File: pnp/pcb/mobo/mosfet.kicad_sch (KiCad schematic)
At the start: 4 parts, among them J25 Mosfet, Q4 AO3400A

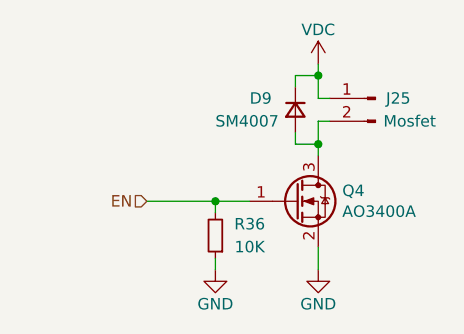
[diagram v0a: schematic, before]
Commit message: replaces SRL05 for SRV05 due to pricing and availability, routed mostfet gate resistors and added 2g34 buffer to boost the voltage of the servo drive pins. consolidated a random cap value that could be switched to an existing one.
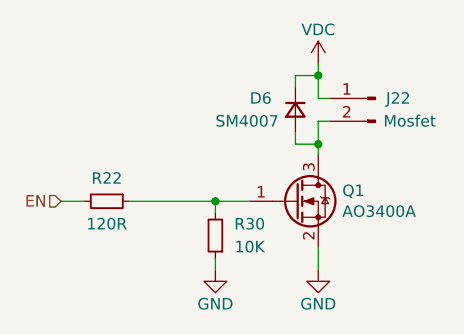
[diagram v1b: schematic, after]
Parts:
- added R22: 120R, Resistor_SMD:R_0805_2012Metric, symbol Device:R_Small
- renumbered D9 to D6, J25 to J22, Q4 to Q1, R36 to R30
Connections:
- net EN: now also R22.2; no longer Q1.1 (G), R30.2
- new net: Q1.1 (G), R22.1, R30.2
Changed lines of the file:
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@@
+    (stroke (width 0) (type default) (color 0 0 0 0))
+  )
+  (wire (pts (xy 123.825 105.41) (xy 126.365 105.41))
     (stroke (width 0) (type default) (color 0 0 0 0))
   )
@@
     (stroke (width 0) (type default) (color 0 0 0 0))
   )
-  (wire (pts (xy 133.35 105.41) (xy 140.97 105.41))
+  (wire (pts (xy 131.445 105.41) (xy 140.97 105.41))
     (stroke (width 0) (type default) (color 0 0 0 0))
   )
-  (hierarchical_label "EN" (shape input) (at 133.35 105.41 180)
+  (hierarchical_label "EN" (shape input) (at 123.825 105.41 180)
     (effects (font (size 1.27 1.27)) (justify right))
   )
   (symbol (lib_id "Connector:Conn_01x02_Male") (at 158.75 93.98 0) (mirror y)
     (in_bom yes) (on_board yes)
-    (property "Reference" "J25" (id 0) (at 161.29 93.98 0))
+    (property "Reference" "J22" (id 0) (at 161.29 93.98 0))
     (property "Value" "Mosfet" (id 1) (at 162.56 96.52 0))
     (property "Footprint" "Connector_JST:JST_XH_B2B-XH-A_1x02_P2.50mm_Vertical" (id 2) (at 158.75 93.98 0)
@@
   (symbol (lib_id "Transistor_FET:AO3400A") (at 149.86 105.41 0)
     (in_bom yes) (on_board yes)
-    (property "Reference" "Q4" (id 0) (at 155.067 104.2416 0)
+    (property "Reference" "Q1" (id 0) (at 155.067 104.2416 0)
       (effects (font (size 1.27 1.27)) (justify left))
     )
@@
   (symbol (lib_id "Device:R_Small") (at 140.97 109.22 180)
     (in_bom yes) (on_board yes)
-    (property "Reference" "R36" (id 0) (at 144.78 107.95 0))
+    (property "Reference" "R30" (id 0) (at 144.78 107.95 0))
     (property "Value" "10K" (id 1) (at 144.78 110.49 0))
     (property "Footprint" "Resistor_SMD:R_0805_2012Metric" (id 2) (at 140.97 109.22 0)
@@
   (symbol (lib_id "Device:D_Small") (at 149.86 95.25 270)
     (in_bom yes) (on_board yes)
-    (property "Reference" "D9" (id 0) (at 144.78 93.98 90)
+    (property "Reference" "D6" (id 0) (at 144.78 93.98 90)
       (effects (font (size 1.27 1.27)) (justify left))
     )
@@
     (pin "1")
   )
+  (symbol (lib_id "Device:R_Small") (at 128.905 105.41 270)
+    (in_bom yes) (on_board yes)
+    (property "Reference" "R22" (id 0) (at 128.905 102.87 90))
+    (property "Value" "120R" (id 1) (at 128.905 107.95 90))
+    (property "Footprint" "Resistor_SMD:R_0805_2012Metric" (id 2) (at 128.905 105.41 0)
+      (effects (font (size 1.27 1.27)) hide)
+    )
+    (property "Datasheet" "https://www.vishay.com/docs/20035/dcrcwe3.pdf" (id 3) (at 128.905 105.41 0)
+      (effects (font (size 1.27 1.27)) hide)
+    )
+    (property "JLCPCB" "C4360" (id 4) (at 128.905 105.41 0)
+      (effects (font (size 1.27 1.27)) hide)
+    )
+    (property "LCSC" "C139879" (id 5) (at 128.905 105.41 0)
+      (effects (font (size 1.27 1.27)) hide)
+    )
+    (property "Digikey" "541-36.0KCCT-ND" (id 6) (at 128.905 105.41 0)
+      (effects (font (size 1.27 1.27)) hide)
+    )
+    (property "Mouser" "71-CRCW080536K0FKEA" (id 7) (at 128.905 105.41 0)
+      (effects (font (size 1.27 1.27)) hide)
+    )
+    (pin "1")
+    (pin "2")
+  )
 )

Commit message: Update mobo schematic with part numbers and ratings
All parts now have part numbers for at least one reseller or manufacturer along with rating specifications.

Note: I did not update the PCB with these new properties, as it seems the PCB is a bit out of sync with the schematic.
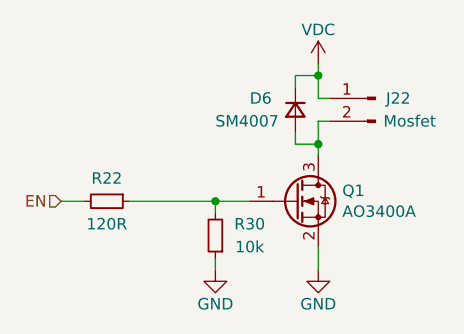
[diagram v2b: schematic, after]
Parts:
- D6: Notes (none) -> 100V/1A
- Q1: Notes (none) -> 30V/5A
- R22: Notes (none) -> 125mW/1%
- R30: value 10K -> 10k; Notes (none) -> 125mW/1%

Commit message: changes footprints for tht connectors, removes stepper driver module in exchange for a dedicated TMC2226 driver implemented on the board
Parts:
- J22: footprint Connector_JST:JST_XH_B2B-XH-A_1x02_P2.50mm_Vertical -> Connector_JST:JST_PH_B2B-PH-SM4-TB_1x02-1MP_P2.00mm_Vertical
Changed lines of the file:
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@@
       (effects (font (size 1.27 1.27)))
     )
-    (property "Footprint" "Connector_JST:JST_XH_B2B-XH-A_1x02_P2.50mm_Vertical" (at 158.75 93.98 0)
+    (property "Footprint" "Connector_JST:JST_PH_B2B-PH-SM4-TB_1x02-1MP_P2.00mm_Vertical" (at 158.75 93.98 0)
       (effects (font (size 1.27 1.27)) hide)
     )

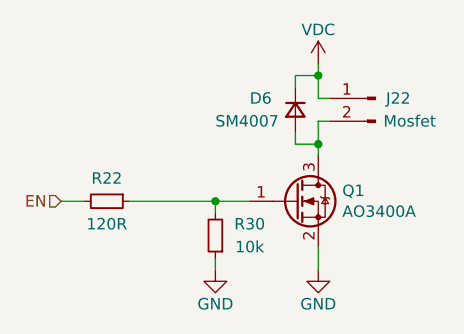
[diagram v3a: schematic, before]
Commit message: Motor driver new Symbol and fix TVS placement
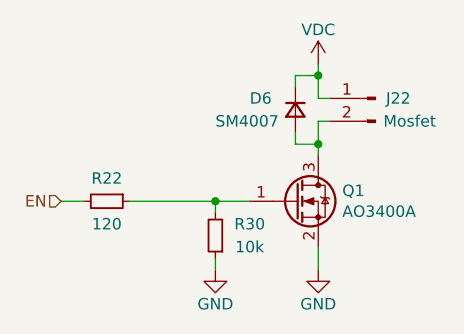
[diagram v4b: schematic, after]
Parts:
- R22: value 120R -> 120
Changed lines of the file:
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@@
   (title_block
     (title "LumenPnP Motherboard")
-    (date "2022-03-29")
-    (rev "003")
+    (date "2023-07-30")
+    (rev "005")
     (company "Opulo")
   )
@@
       (effects (font (size 1.27 1.27)))
     )
-    (property "Value" "120R" (at 128.905 107.95 90)
-      (effects (font (size 1.27 1.27)))
-    )
+    (property "Value" "120" (at 128.905 107.95 90)
+      (effects (font (size 1.27 1.27)))
+    )

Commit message: All pages checked
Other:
- moved on the sheet: D6, J22, Q1, R22, R30

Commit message: Mobo parts sourced
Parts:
- J22: JLCPCB C20079 -> C2845451; LCSC C20079 -> C2845451
- Q1: JLCPCB C332101 -> C20917
- R22: JLCPCB C4360 -> C17437; LCSC C139879 -> C17437; Notes 125mW/1% -> (none)
- R30: JLCPCB C4360 -> C17414; LCSC C139879 -> C17414; Notes 125mW/1% -> (none)
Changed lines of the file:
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@@
       (effects (font (size 1.27 1.27)) hide)
     )
-    (property "JLCPCB" "C20079" (at 113.665 60.96 0)
-      (effects (font (size 1.27 1.27)) hide)
-    )
-    (property "LCSC" "C20079" (at 113.665 60.96 0)
+    (property "JLCPCB" "C2845451" (at 113.665 60.96 0)
+      (effects (font (size 1.27 1.27)) hide)
+    )
+    (property "LCSC" "C2845451" (at 113.665 60.96 0)
       (effects (font (size 1.27 1.27)) hide)
     )
@@
       (effects (font (size 1.27 1.27)) hide)
     )
-    (property "JLCPCB" "C332101" (at 104.775 72.39 0)
+    (property "JLCPCB" "C20917" (at 104.775 72.39 0)
       (effects (font (size 1.27 1.27)) hide)
     )
@@
       (effects (font (size 1.27 1.27)) hide)
     )
-    (property "JLCPCB" "C4360" (at 95.885 76.2 0)
-      (effects (font (size 1.27 1.27)) hide)
-    )
-    (property "LCSC" "C139879" (at 95.885 76.2 0)
+    (property "JLCPCB" "C17414" (at 95.885 76.2 0)
+      (effects (font (size 1.27 1.27)) hide)
+    )
+    (property "LCSC" "C17414" (at 95.885 76.2 0)
       (effects (font (size 1.27 1.27)) hide)
     )
@@
       (effects (font (size 1.27 1.27)) hide)
     )
-    (property "Notes" "125mW/1%" (at 95.885 76.2 0)
+    (property "Notes" "" (at 95.885 76.2 0)
       (effects (font (size 1.27 1.27)) hide)
     )
@@
       (effects (font (size 1.27 1.27)) hide)
     )
-    (property "JLCPCB" "C4360" (at 83.82 72.39 0)
-      (effects (font (size 1.27 1.27)) hide)
-    )
-    (property "LCSC" "C139879" (at 83.82 72.39 0)
+    (property "JLCPCB" "C17437" (at 83.82 72.39 0)
+      (effects (font (size 1.27 1.27)) hide)
+    )
+    (property "LCSC" "C17437" (at 83.82 72.39 0)
       (effects (font (size 1.27 1.27)) hide)
     )
@@
       (effects (font (size 1.27 1.27)) hide)
     )
-    (property "Notes" "125mW/1%" (at 83.82 72.39 0)
-      (effects (font (size 1.27 1.27)) hide)
-    )
+    (property "Notes" "" (at 83.82 72.39 0)
+      (effects (font (size 1.27 1.27)) hide)
+    )

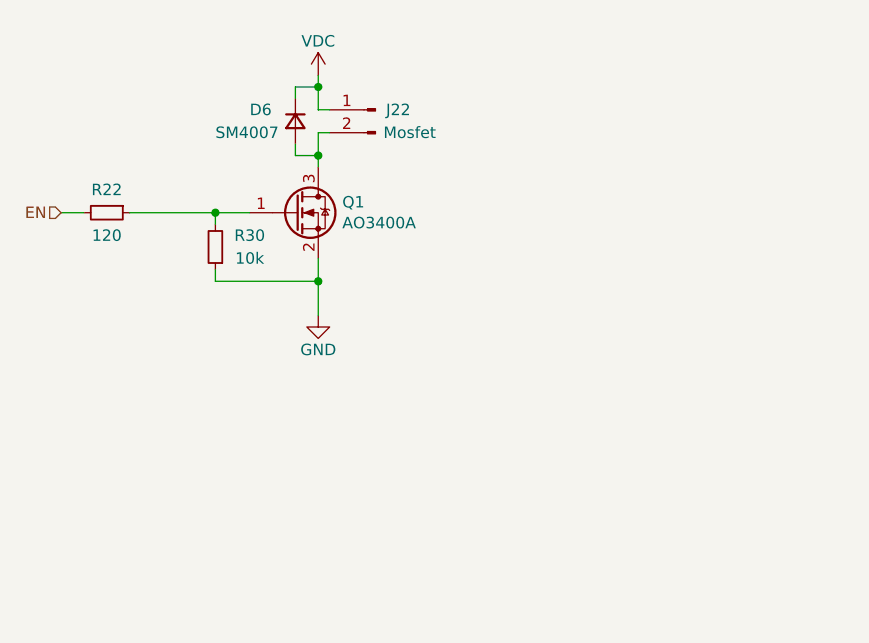
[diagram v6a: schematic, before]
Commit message: Schematic almost finished
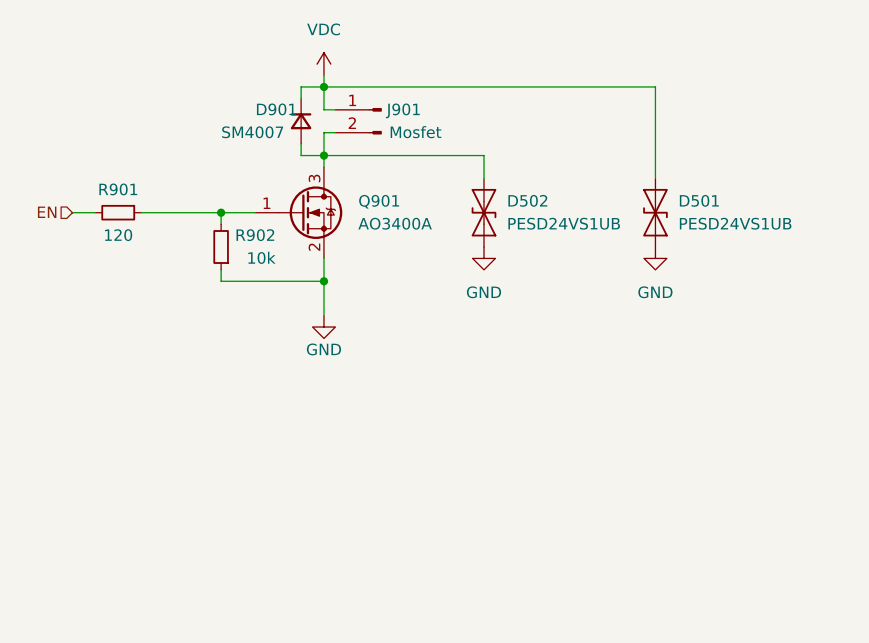
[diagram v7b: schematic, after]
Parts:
- removed Q1: AO3400A, Package_TO_SOT_SMD:SOT-23, symbol Transistor_FET:AO3400A
- added D501, D502: PESD24VS1UB, Diode_SMD:D_SOD-523, symbol Diode:SZESD9B5.0ST5G
- added Q901: AO3400A, Package_TO_SOT_SMD:SOT-23, symbol Transistor_FET:AO3400A
- J901: renamed from J22; symbol Connector:Conn_01x02_Male -> Connector:Conn_01x02_Pin
- renumbered D6 to D901, R22 to R901, R30 to R902
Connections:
- net GND: now also D501.1 (A1), D502.1 (A1), Q901.2 (S)
- net VDC: now also D501.2 (A2)
- net at D901.2 (A), J901.2 (Pin_2): now also D502.2 (A2), Q901.3 (D)
- net at R901.1, R902.2: now also Q901.1 (G)
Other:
- moved on the sheet: D901, J901, R901, R902

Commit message: Finished reverse polarity and inrush current circuits
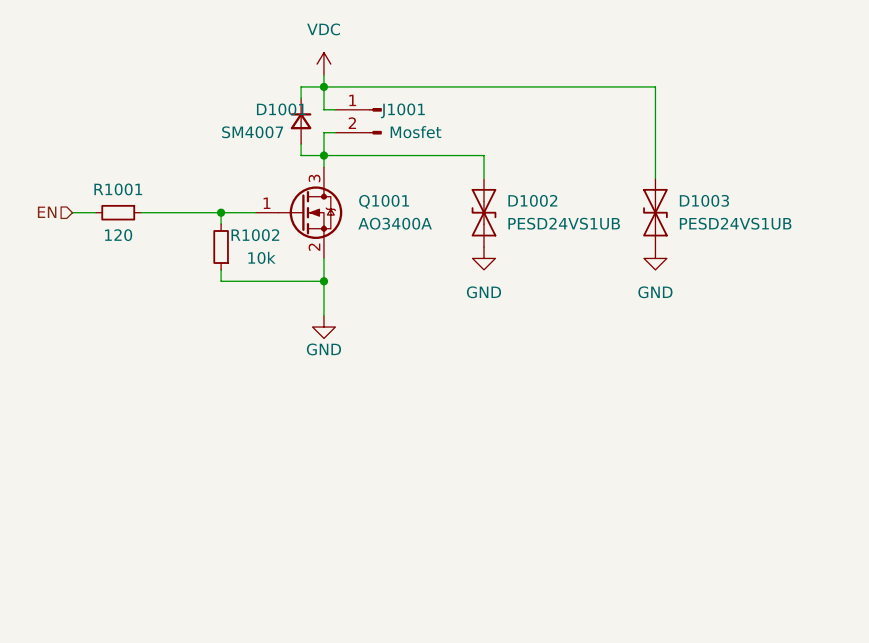
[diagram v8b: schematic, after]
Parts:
- renumbered D901 to D1001, D502 to D1002, D501 to D1003, J901 to J1001, Q901 to Q1001, R901 to R1001, R902 to R1002
